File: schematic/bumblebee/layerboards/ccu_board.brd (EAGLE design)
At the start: 160 x 100 mm, 10 parts, among them IC1 REG1117, P1 B4B-EH-A

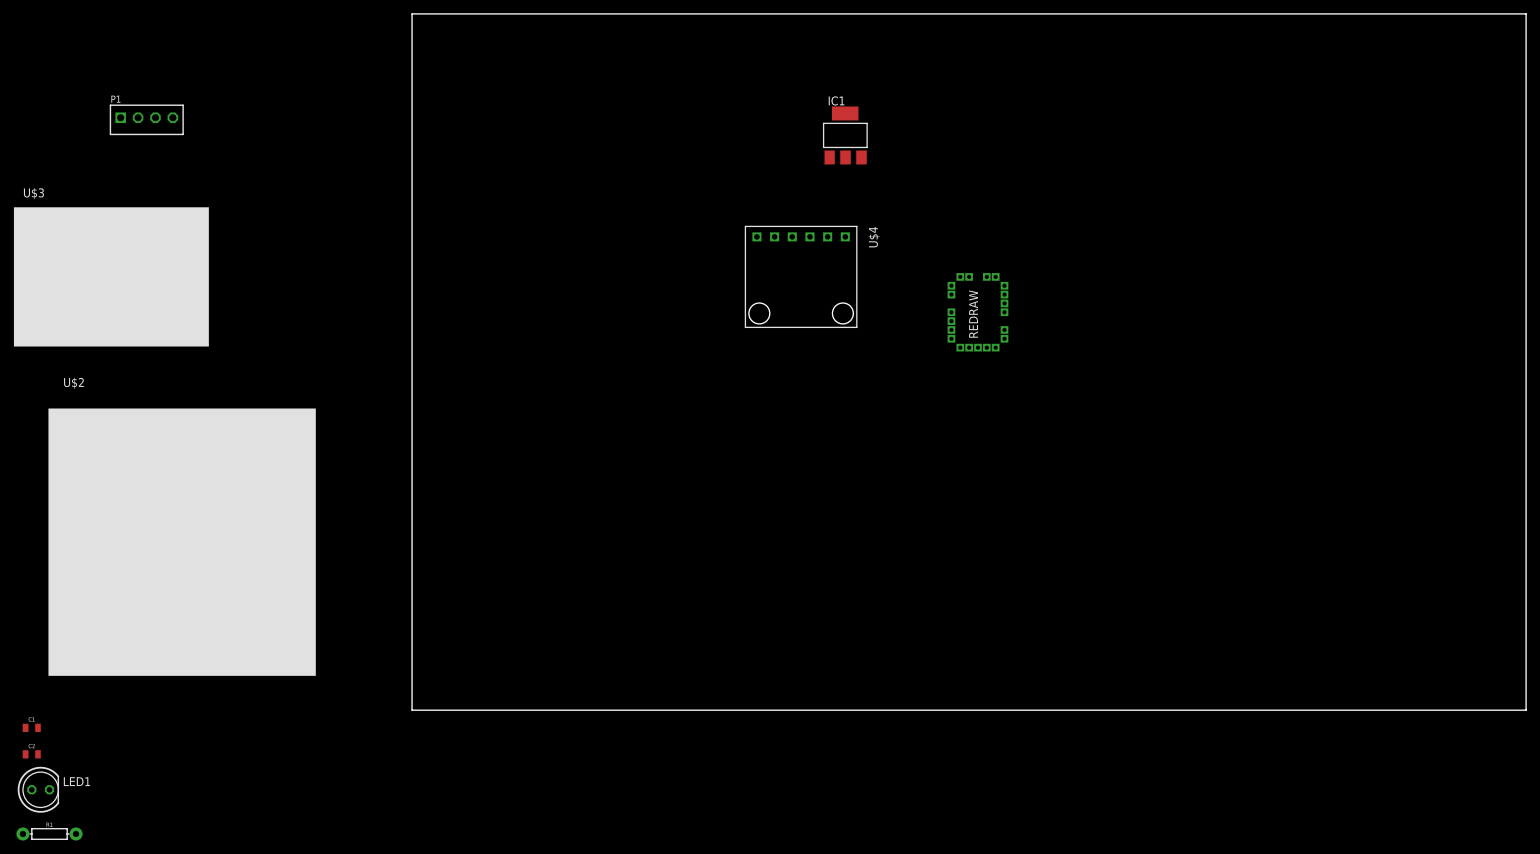
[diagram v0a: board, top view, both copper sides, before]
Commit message: Ведётся работа по платам. Готовы SCU и CCU
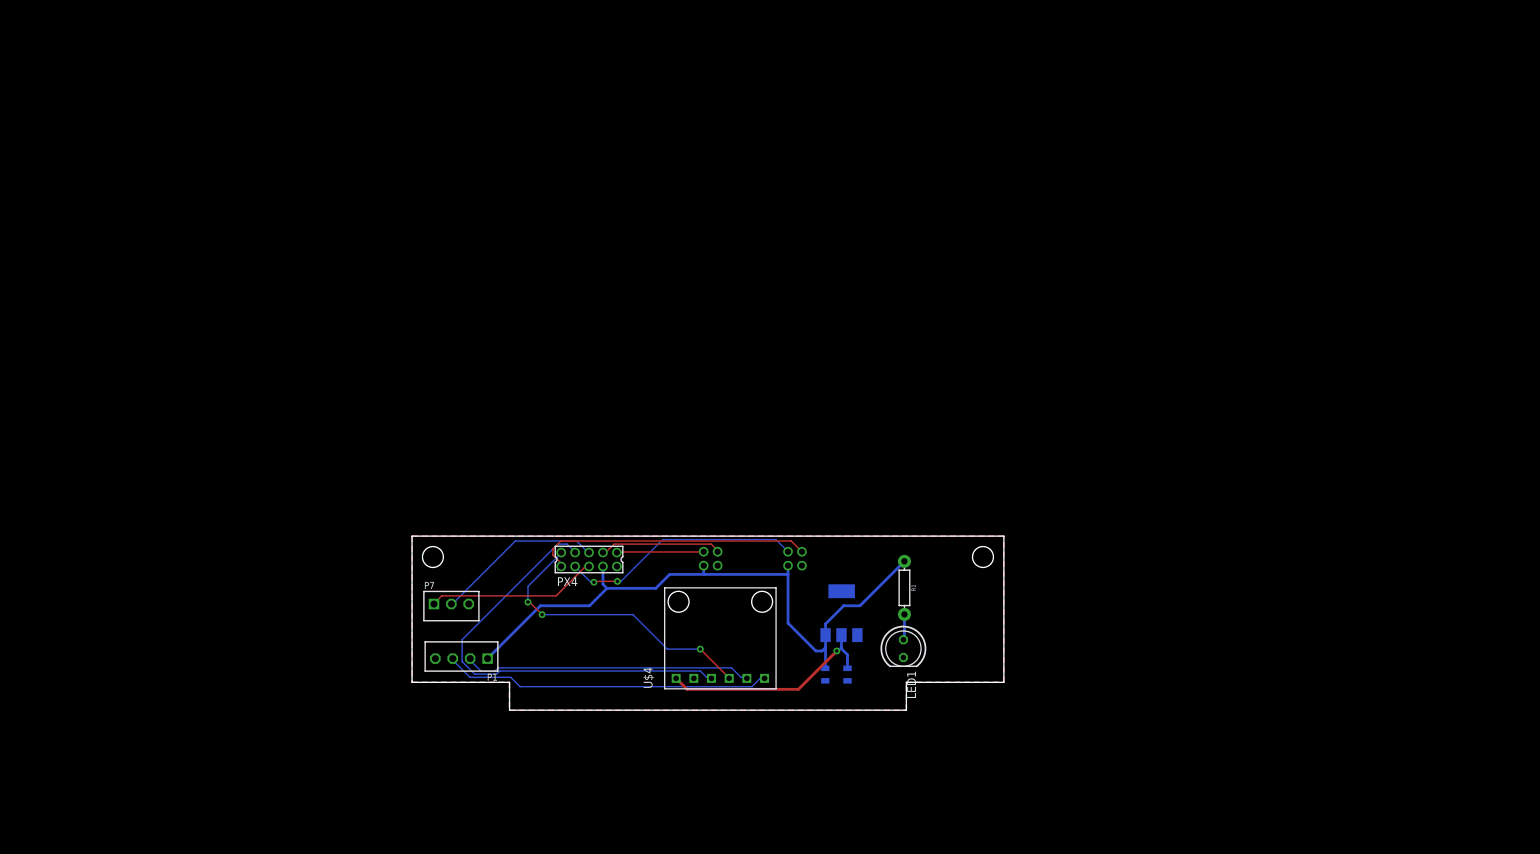
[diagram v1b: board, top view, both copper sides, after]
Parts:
- removed U$1: PX4FLOW, bluepill:PX4FLOW_TMP
- removed U$2: CAM_BIG, bluepill:CAM_BIG
- removed U$3: CAM, bluepill:CAM
- added CAM_B, CAM_S: (no value), con-molex:87758-0416
- added P7: B3B-EH-A, con-jst-eh:B3B-EH-A
- added PX4: (no value), con-molex:87758-1016
- moved R1 127.8 mm to (70.7, 17.6), turned to 270 degrees
- moved LED1 125.6 mm to (70.6, 8.84), turned to 270 degrees
- moved C1 117.4 mm to (62.5, 5.11), flipped to the bottom, turned to 270 degrees
- moved C2 114.5 mm to (59.4, 5.11), flipped to the bottom, turned to 270 degrees
- moved P1 89.9 mm to (7.10, 7.41), turned to 180 degrees
- moved IC1 68.6 mm to (61.7, 13.9), flipped to the bottom
- moved U$4 53.2 mm to (44.3, 10.3), turned to 90 degrees
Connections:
- removed net N$1: U$1.P$16, U$2.TX
- removed net N$2: U$1.P$17, U$2.RX
- removed net N$3: U$1.P$12, U$3.TX
- removed net N$4: U$1.P$13, U$3.RX
- removed net N$5: U$1.P$18, U$4.CTX
- removed net N$7: U$1.P$19, U$4.CRX
- new net CRX: PX4.2, U$4.CRX
- new net CTX: PX4.4, U$4.CTX
- new net RX1: CAM_B.4, PX4.3
- new net RX2: CAM_S.4, PX4.10
- new net SWC: P7.2, PX4.6
- new net SWD: P7.1, PX4.5
- new net TX1: CAM_B.2, PX4.1
- new net TX2: CAM_S.2, PX4.8
- net 5V_CCU: now also CAM_B.3, CAM_S.3, PX4.7; no longer U$1.P$1, U$2.5V, U$3.5V
- net GND: now also CAM_B.1, CAM_S.1, PX4.9; no longer U$1.P$2, U$2.GND, U$3.GND
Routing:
- net 5V_CCU: track 0.00 -> 89.8 mm
- net CTX: track 0.00 -> 62.8 mm
- net N$6: track 0.00 -> 47.1 mm
- net CRX: track 0.00 -> 42.5 mm, vias 0 -> 3
- net N$8: track 0.00 -> 41.4 mm
- net TX1: track 0.00 -> 39.9 mm
- net RX1: track 0.00 -> 34.8 mm, vias 0 -> 2
- net 3V3: track 0.00 -> 32.0 mm, vias 0 -> 1
- net SWD: track 0.00 -> 24.5 mm
- net SWC: track 0.00 -> 24.2 mm
- net TX2: track 0.00 -> 17.5 mm
- net RX2: track 0.00 -> 12.5 mm
- net N$11: track 0.00 -> 3.71 mm
- added copper zone on layer 1, net GND
- added copper zone on layer 16, net GND
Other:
- board size 160 x 100 mm -> 85 x 25 mm

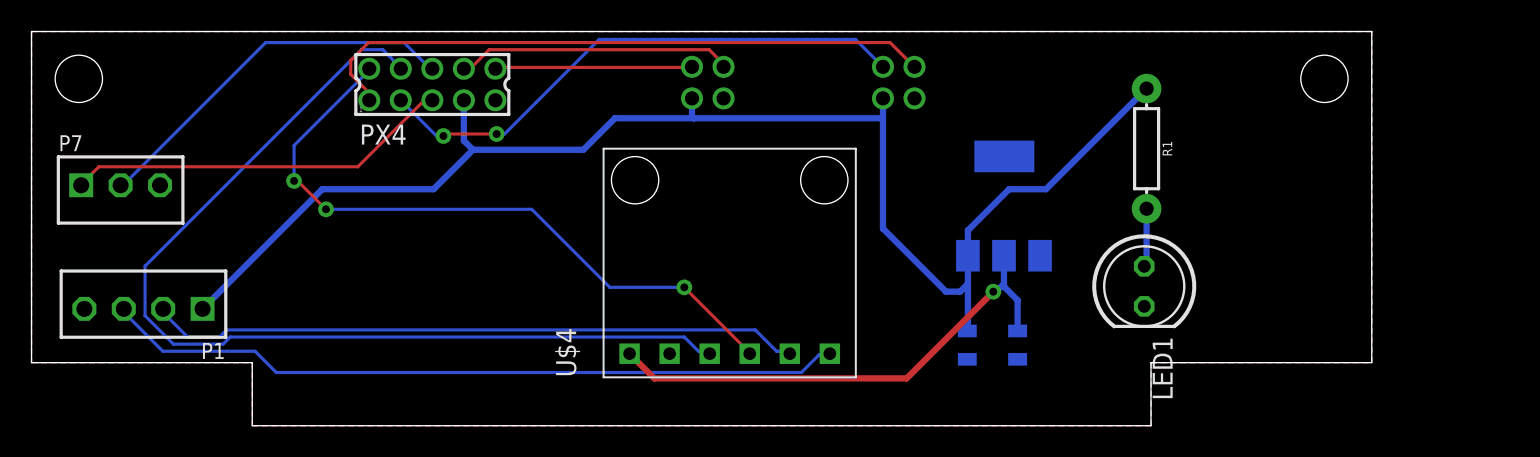
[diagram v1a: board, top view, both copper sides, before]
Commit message: CCU и ICU полностью готовы. Было бы здорово, если бы ещё кто-то посмотрел По SCU требуются уточнения
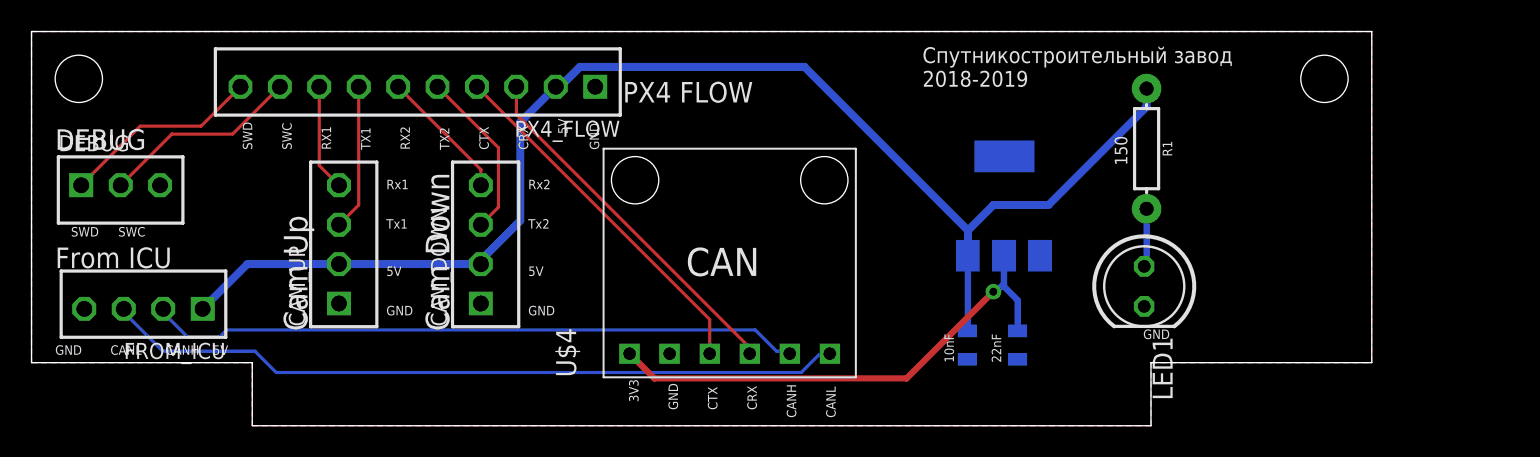
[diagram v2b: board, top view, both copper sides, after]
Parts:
- removed CAM_B, CAM_S: (no value), con-molex:87758-0416
- removed PX4: (no value), con-molex:87758-1016
- added CAM_DOWN, CAM_UP: B4B-EH-A, con-jst-eh:B4B-EH-A
- added PX4_FLOW: B10B-EH-A, con-jst-eh:B10B-EH-A
- renumbered P1 to FROM_ICU, P7 to DEBUG
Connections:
- net 5V_CCU: now also CAM_DOWN.2, CAM_UP.2, PX4_FLOW.2; no longer CAM_B.3, CAM_S.3, PX4.7
- net CRX: now also PX4_FLOW.3; no longer PX4.2
- net CTX: now also PX4_FLOW.4; no longer PX4.4
- net GND: now also CAM_DOWN.1, CAM_UP.1, PX4_FLOW.1; no longer CAM_B.1, CAM_S.1, PX4.9
- net RX1: now also CAM_UP.4, PX4_FLOW.8; no longer CAM_B.4, PX4.3
- net RX2: now also CAM_DOWN.4, PX4_FLOW.6; no longer CAM_S.4, PX4.10
- net SWC: now also PX4_FLOW.9; no longer PX4.6
- net SWD: now also PX4_FLOW.10; no longer PX4.5
- net TX1: now also CAM_UP.3, PX4_FLOW.7; no longer CAM_B.2, PX4.1
- net TX2: now also CAM_DOWN.3, PX4_FLOW.5; no longer CAM_S.2, PX4.8
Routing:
- net CTX: track 62.8 -> 23.0 mm
- net TX1: track 39.9 -> 9.27 mm
- net RX1: track 34.8 -> 6.77 mm, vias 2 -> 0
- net CRX: track 42.5 -> 23.1 mm, vias 3 -> 0
- net SWD: track 24.5 -> 12.7 mm
- net SWC: track 24.2 -> 12.7 mm
- net TX2: track 17.5 -> 10.8 mm
- net 5V_CCU: track 89.8 -> 85.1 mm
- net RX2: track 12.5 -> 8.42 mm
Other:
- board text added: "10nF"
- board text added: "150"
- board text added: "22nF"
- board text added: "3V3"
- board text added: "5V"
- board text added: "CAN"
- board text added: "CANH"
- board text added: "CANL"
- board text added: "CRX"
- board text added: "CTX"
- board text added: "Cam Down"
- board text added: "Cam Up"
- board text added: "DEBUG"
- board text added: "From ICU"
- board text added: "GND"
- board text added: "PX4 FLOW"
- board text added: "RX1"
- board text added: "RX2"
- board text added: "Rx1"
- board text added: "Rx2"
- board text added: "SWC"
- board text added: "SWD"
- board text added: "TX1"
- board text added: "TX2"
- board text added: "Tx1"
- board text added: "Tx2"
- board text added: "Спутникостроительный завод 2018-2019"

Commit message: Подготовка плат к производству
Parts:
- renumbered IC1 to LDO, U$4 to CAN
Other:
- board text removed: "CAN"
- board text removed: "Cam Down"
- board text removed: "Cam Up"
- board text removed: "DEBUG"
- board text removed: "From ICU"
- board text removed: "PX4 FLOW"
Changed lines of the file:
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@@
 <?xml version="1.0" encoding="utf-8"?>
 <!DOCTYPE eagle SYSTEM "eagle.dtd">
-<eagle version="9.3.0">
+<eagle version="9.3.2">
 <drawing>
 <settings>
@@
 <layer number="25" name="tNames" color="7" fill="1" visible="yes" active="yes"/>
 <layer number="26" name="bNames" color="7" fill="1" visible="yes" active="yes"/>
-<layer number="27" name="tValues" color="7" fill="1" visible="yes" active="yes"/>
-<layer number="28" name="bValues" color="7" fill="1" visible="yes" active="yes"/>
+<layer number="27" name="tValues" color="7" fill="1" visible="no" active="yes"/>
+<layer number="28" name="bValues" color="7" fill="1" visible="no" active="yes"/>
 <layer number="29" name="tStop" color="7" fill="3" visible="no" active="yes"/>
 <layer number="30" name="bStop" color="7" fill="6" visible="no" active="yes"/>
@@
 <wire x1="85" y1="4" x2="71" y2="4" width="0" layer="20"/>
 <wire x1="71" y1="4" x2="71" y2="0" width="0" layer="20"/>
-<text x="17.5" y="6" size="1.5" layer="21" rot="R90">Cam Up</text>
-<text x="26.5" y="6" size="1.5" layer="21" rot="R90">Cam Down</text>
 <text x="22.5" y="15" size="0.6" layer="21">Rx1</text>
 <text x="31.5" y="15" size="0.6" layer="21">Rx2</text>
@@
 <text x="22.5" y="7" size="0.6" layer="21">GND</text>
 <text x="31.5" y="7" size="0.6" layer="21">GND</text>
-<text x="41.5" y="9.5" size="1.778" layer="21">CAN</text>
 <text x="38.5" y="1.5" size="0.6" layer="21" rot="R90">3V3</text>
 <text x="41" y="1" size="0.6" layer="21" rot="R90">GND</text>
@@
 <text x="58.5" y="4" size="0.6" layer="21" rot="R90">10nF</text>
 <text x="61.5" y="4" size="0.6" layer="21" rot="R90">22nF</text>
-<text x="1.5" y="17.5" size="1.3" layer="21">DEBUG</text>
-<text x="1.5" y="10" size="1.3" layer="21">From ICU</text>
-<text x="37.5" y="20.5" size="1.3" layer="21">PX4 FLOW</text>
 <text x="36" y="17.5" size="0.6" layer="21" rot="R90">GND</text>
 <text x="34" y="18.5" size="0.6" layer="21" rot="R90">5V</text>
@@
 <param name="mlMinCreamFrame" value="0mil"/>
 <param name="mlMaxCreamFrame" value="0mil"/>
-<param name="mlViaStopLimit" value="0mil"/>
+<param name="mlViaStopLimit" value="0.6mm"/>
 <param name="srRoundness" value="0"/>
 <param name="srMinRoundness" value="0mil"/>
@@
 </autorouter>
 <elements>
-<element name="IC1" library="burr-brown" library_urn="urn:adsk.eagle:library:111" package="SOT223" package3d_urn="urn:adsk.eagle:package:4940/1" value="REG1117" x="61.7" y="13.93" smashed="yes" rot="MR0">
+<element name="LDO" library="burr-brown" library_urn="urn:adsk.eagle:library:111" package="SOT223" package3d_urn="urn:adsk.eagle:package:4940/1" value="REG1117" x="61.7" y="13.93" smashed="yes" rot="MR0">
 <attribute name="MF" value="" x="42.65" y="-72.43" size="1.778" layer="28" rot="MR0" display="off"/>
 <attribute name="MPN" value="REG1117" x="42.65" y="-72.43" size="1.778" layer="28" rot="MR0" display="off"/>
@@
 </element>
 <element name="FROM_ICU" library="con-jst-eh" package="B4B-EH-A" value="B4B-EH-A" x="7.1" y="7.41" smashed="yes" rot="R180">
-<attribute name="NAME" x="12.307" y="5.251" size="1.016" layer="25" ratio="18" rot="R180"/>
+<attribute name="NAME" x="12.307" y="11.251" size="1.016" layer="25" ratio="18" rot="R180"/>
 <attribute name="VALUE" x="12.307" y="11.093" size="1.016" layer="27" ratio="10" rot="R180"/>
 </element>
-<element name="U$4" library="bluepill" package="CAN" value="CAN" x="44.28" y="10.32" smashed="yes" rot="R90">
-<attribute name="NAME" x="34.54" y="3.07" size="1.27" layer="25" rot="R90"/>
+<element name="CAN" library="bluepill" package="CAN" value="CAN" x="44.28" y="10.32" smashed="yes" rot="R90">
+<attribute name="NAME" x="46.43" y="11.04" size="1.27" layer="25" rot="R180"/>
 <attribute name="VALUE" x="54.9" y="3.31" size="1.27" layer="27" rot="R90"/>
 </element>
@@
 </element>
 <element name="LED1" library="led" library_urn="urn:adsk.eagle:library:259" package="LED5MM" package3d_urn="urn:adsk.eagle:package:15799/2" value="" x="70.57" y="8.84" smashed="yes" rot="R270">
-<attribute name="NAME" x="71.1034" y="5.665" size="1.27" layer="25" ratio="10" rot="R270"/>
+<attribute name="NAME" x="75.1034" y="10.665" size="1.27" layer="25" ratio="10" rot="R270"/>
 <attribute name="VALUE" x="68.7666" y="5.6396" size="1.27" layer="27" ratio="10" rot="R270"/>
 </element>
@@
 </element>
 <element name="PX4_FLOW" library="con-jst-eh" package="B10B-EH-A" value="B10B-EH-A" x="24.5" y="21.5" smashed="yes" rot="R180">
-<attribute name="NAME" x="37.327" y="19.341" size="1.016" layer="25" ratio="18" rot="R180"/>
+<attribute name="NAME" x="44.827" y="21.841" size="1.016" layer="25" ratio="18" rot="R180"/>
 <attribute name="VALUE" x="37.327" y="25.183" size="1.016" layer="27" ratio="10" rot="R180"/>
 </element>
@@
 <signal name="5V_CCU">
 <contactref element="FROM_ICU" pad="1"/>
-<contactref element="IC1" pad="3"/>
+<contactref element="LDO" pad="3"/>
 <contactref element="C2" pad="1"/>
 <contactref element="R1" pad="P$1"/>
@@
 <signal name="GND">
 <contactref element="FROM_ICU" pad="4"/>
-<contactref element="IC1" pad="1"/>
+<contactref element="LDO" pad="1"/>
 <contactref element="C1" pad="2"/>
 <contactref element="C2" pad="2"/>
 <contactref element="LED1" pad="K"/>
-<contactref element="U$4" pad="GND"/>
+<contactref element="CAN" pad="GND"/>
 <polygon width="0.2" layer="16">
 <vertex x="0" y="25"/>
@@
 </signal>
 <signal name="N$6">
-<contactref element="U$4" pad="CANL"/>
+<contactref element="CAN" pad="CANL"/>
 <contactref element="FROM_ICU" pad="3"/>
 <wire x1="49.95" y1="4.5" x2="50.625" y2="4.5" width="0.2" layer="16"/>
-<wire x1="48.825" y1="3.375" x2="49.95" y2="4.5" width="0.2" layer="16"/>
-<wire x1="15.525" y1="3.375" x2="48.825" y2="3.375" width="0.2" layer="16"/>
-<wire x1="14.175" y1="4.725" x2="15.525" y2="3.375" width="0.2" layer="16"/>
-<wire x1="8.325" y1="4.725" x2="14.175" y2="4.725" width="0.2" layer="16"/>
-<wire x1="5.85" y1="7.2" x2="8.325" y2="4.725" width="0.2" layer="16"/>
+<wire x1="48.325" y1="2.875" x2="49.95" y2="4.5" width="0.2" layer="16"/>
+<wire x1="18.025" y1="2.875" x2="48.325" y2="2.875" width="0.2" layer="16"/>
+<wire x1="15.675" y1="5.225" x2="18.025" y2="2.875" width="0.2" layer="16"/>
+<wire x1="7.825" y1="5.225" x2="15.675" y2="5.225" width="0.2" layer="16"/>
+<wire x1="5.85" y1="7.2" x2="7.825" y2="5.225" width="0.2" layer="16"/>
 <wire x1="50.625" y1="4.5" x2="50.63" y2="4.57" width="0.2" layer="16"/>
 <wire x1="5.85" y1="7.2" x2="5.85" y2="7.41" width="0.2" layer="16"/>
 </signal>
 <signal name="N$8">
-<contactref element="U$4" pad="CANH"/>
+<contactref element="CAN" pad="CANH"/>
 <contactref element="FROM_ICU" pad="2"/>
 <wire x1="47.25" y1="4.725" x2="47.925" y2="4.725" width="0.2" layer="16"/>
 <wire x1="45.9" y1="6.075" x2="47.25" y2="4.725" width="0.2" layer="16"/>
-<wire x1="12.375" y1="6.075" x2="45.9" y2="6.075" width="0.2" layer="16"/>
-<wire x1="11.925" y1="5.625" x2="12.375" y2="6.075" width="0.2" layer="16"/>
-<wire x1="9.9" y1="5.625" x2="11.925" y2="5.625" width="0.2" layer="16"/>
-<wire x1="8.325" y1="7.2" x2="9.9" y2="5.625" width="0.2" layer="16"/>
+<wire x1="9.45" y1="6.075" x2="45.9" y2="6.075" width="0.2" layer="16"/>
+<wire x1="8.325" y1="7.2" x2="9.45" y2="6.075" width="0.2" layer="16"/>
 <wire x1="47.925" y1="4.725" x2="48.09" y2="4.57" width="0.2" layer="16"/>
 <wire x1="8.325" y1="7.2" x2="8.35" y2="7.41" width="0.2" layer="16"/>
 </signal>
 <signal name="3V3">
-<contactref element="U$4" pad="3V3"/>
-<contactref element="IC1" pad="2"/>
+<contactref element="CAN" pad="3V3"/>
+<contactref element="LDO" pad="2"/>
 <contactref element="C1" pad="1"/>
 <wire x1="61.6746" y1="10.7804" x2="61.6746" y2="9" width="0.4" layer="16"/>
@@
 </signal>
 <signal name="CRX">
-<contactref element="U$4" pad="CRX"/>
+<contactref element="CAN" pad="CRX"/>
 <contactref element="PX4_FLOW" pad="3"/>
-<wire x1="30.75" y1="21.5" x2="30.75" y2="19.75" width="0.2" layer="1"/>
-<wire x1="45.55" y1="4.95" x2="45.55" y2="4.57" width="0.2" layer="1"/>
-<wire x1="30.75" y1="19.75" x2="45.55" y2="4.95" width="0.2" layer="1"/>
+<wire x1="30.75" y1="21.5" x2="30.75" y2="18.75" width="0.2" layer="1"/>
+<wire x1="45.55" y1="4.57" x2="44.93" y2="4.57" width="0.2" layer="1"/>
+<wire x1="44.93" y1="4.57" x2="30.75" y2="18.75" width="0.2" layer="1"/>
 </signal>
 <signal name="CTX">
-<contactref element="U$4" pad="CTX"/>
+<contactref element="CAN" pad="CTX"/>
 <contactref element="PX4_FLOW" pad="4"/>
-<wire x1="28.25" y1="21.5" x2="43.01" y2="6.74" width="0.2" layer="1"/>
-<wire x1="43.01" y1="6.74" x2="43.01" y2="4.57" width="0.2" layer="1"/>
+<wire x1="43.01" y1="5.24" x2="28.25" y2="20" width="0.2" layer="1"/>
+<wire x1="28.25" y1="21.5" x2="28.25" y2="20" width="0.2" layer="1"/>
+<wire x1="43.01" y1="5.24" x2="43.01" y2="4.57" width="0.2" layer="1"/>
 </signal>
 <signal name="SWD">
